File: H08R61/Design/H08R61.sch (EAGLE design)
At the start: 28 parts, among them P1 HEXABIT_17.32, U2 VL53L0X, X1 XTALL_CSTCE8M00G52

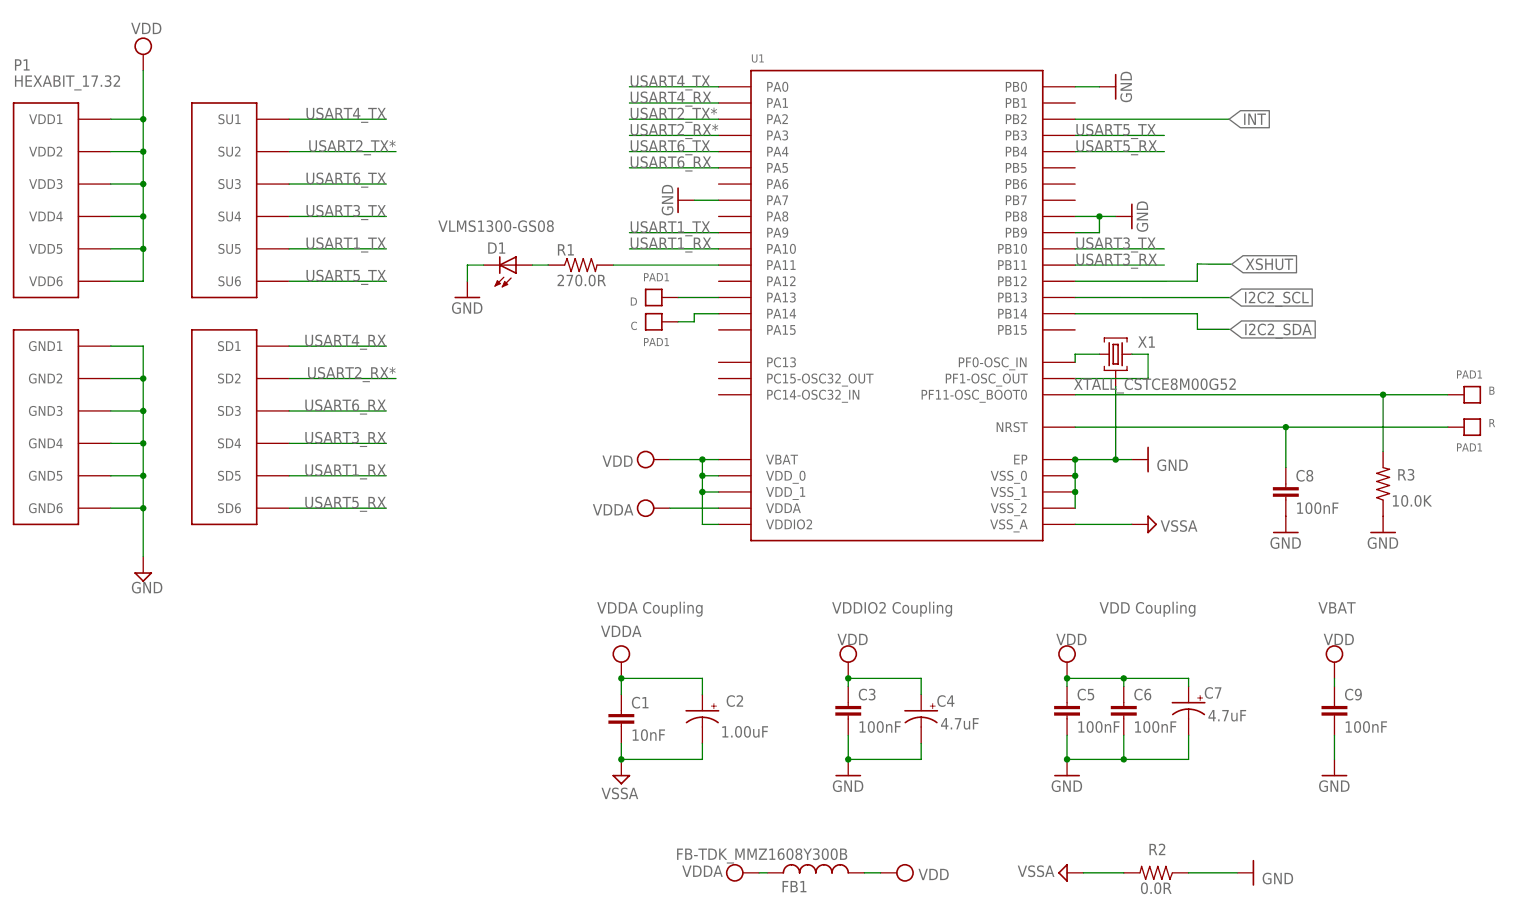
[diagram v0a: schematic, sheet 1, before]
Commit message: - Changing the MC to STM32G0 - Editing the electronic design to improve the performance
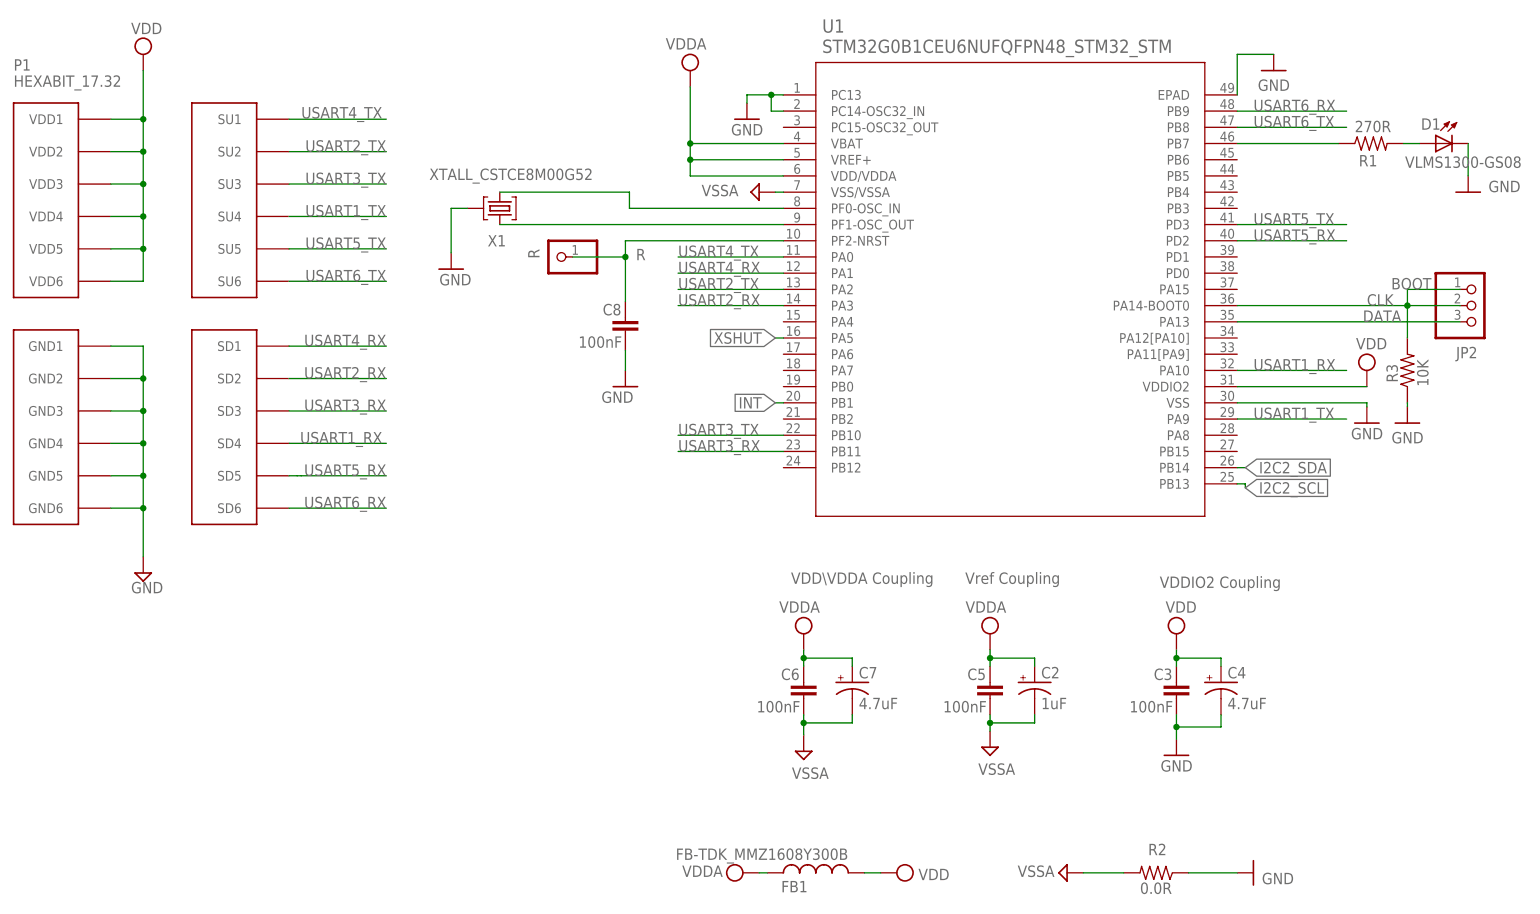
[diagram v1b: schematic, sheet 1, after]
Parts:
- removed B, C, D: PAD1, Hexabitz:PAD1
- removed C1: 10nF, Hexabitz:C-0603
- removed C9: 100nF, Hexabitz:C-0603
- removed R4: 2.2k, Hexabitz:R-0603
- added JP2: (no value), pinhead:PINHD-1X3
- added R8: 10k, HEXABITZ_RCLS:R-0603
- C10: device Hexabitz:C-0603 -> HEXABITZ_RCLS:C-0603; CAPACITANCE 100 nF -> (none); MFN KEMET -> (none); MPN C0603C104K8RACTU -> (none); OCTOPART_URL https://octopart.com/0603yc104k4t2a-avx+interconnect+%2F+el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 -> (none); TOLERANCE ±10% -> (none); VOLTAGE_RATING 16.0 V -> (none)
- C11: device Hexabitz:C-0805 -> HEXABITZ_RCLS:C-0805-POL; CAPACITANCE 4.7µF -> (none); MFN Murata -> (none); MPN GRM21BC81E475KA12L -> (none); OCTOPART_URL https://octopart.com/grm21bc81e475ka12l-murata-10331911?r=s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 -> (none); TOLERANCE 10% -> (none); VOLTAGE_RATING 25V -> (none)
- C2: value 1.00uF -> 1uF; device Hexabitz:C-0805 -> HEXABITZ_RCLS:C-0805-POL; CAPACITANCE 1.00uF -> (none); MFN Yageo -> (none); MPN CC0805KKX7R7BB105 -> (none); OCTOPART_URL https://octopart.com/cc0805kkx7r7bb105-yageo-8376555?r=sp&s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 -> (none); TOLERANCE 10% -> (none); VOLTAGE_RATING 16V -> (none)
- C3, C6, C8: device Hexabitz:C-0603 -> HEXABITZ_RCLS:C-0603; CAPACITANCE 100nF -> (none); MFN KEMET -> (none); MPN C0603C104K8RACTU -> (none); OCTOPART_URL https://octopart.com/c0603c104k8ractu-kemet-145075?r=sp&s=9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 -> (none); TOLERANCE 10% -> (none); VOLTAGE_RATING 10V -> (none)
- C4, C7: device Hexabitz:C-0805 -> HEXABITZ_RCLS:C-0805-POL; CAPACITANCE 4.7uF -> (none); MFN Murata -> (none); MPN GRM21BC81E475KA12L -> (none); OCTOPART_URL https://octopart.com/grm21bc81e475ka12l-murata-10331911?r=s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 -> (none); TOLERANCE 10% -> (none); VOLTAGE_RATING 25V -> (none)
- C5: device Hexabitz:C-0603 -> HEXABITZ_RCLS:C-0603; CAPACITANCE 100nF -> (none); MFN KEMET -> (none); MPN C0603C104K8RACTU -> (none); OCTOPART_URL https://octopart.com/c0603c104k8ractu-kemet-145075?r=sp&s=9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 -> (none); TOLERANCE 10% -> (none); VOLTAGE_RATING 10 -> (none)
- FB1: device Hexabitz:FB-TDK_MMZ1608Y300B -> HEXABITZ_RCLS:FB-TDK_MMZ1608Y300B
- R: value PAD1 -> R; device Hexabitz:PAD1 -> HEXABITZ_USER_INTERFACE_PARTS:PINHD-1X1
- R1: value 270.0R -> 270R; device Hexabitz:R-0603 -> HEXABITZ_RCLS:R-0603; MFN Yageo -> (none); MPN RC0603FR-07270RL -> (none); OCTOPART_URL https://octopart.com/erj-3geyj271v-panasonic-55560546 -> (none); RESISTANCE 270.0 Ohm -> (none); TOLERANCE 1% -> (none)
- R2: device Hexabitz:R-0603 -> HEXABITZ_RCLS:R-0603; OCTOPART_URL https://octopart.com/crcw06030000z0eahp-vishay-44320230 -> https://octopart.com/rc0603jr-070rl-yageo-1241539?r=sp&s=X2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
- R3: value 10.0K -> 10K; device Hexabitz:R-0603 -> HEXABITZ_RCLS:R-0603; MFN Yageo -> (none); MPN RC0603JR-0710KL -> (none); OCTOPART_URL https://octopart.com/crcw060310k0jneb-vishay+dale-46603268 -> (none); RESISTANCE 10.0K Ohm -> (none); TOLERANCE 5% -> (none)
- R5, R6: device Hexabitz:R-0603 -> HEXABITZ_RCLS:R-0603; MFN Yageo -> (none); MPN RC0603FR-07270RL -> (none); OCTOPART_URL https://octopart.com/crcw06032k20fkea-vishay-40018987 -> (none); RESISTANCE 2.2 kΩ -> (none); TOLERANCE ±1% -> (none)
- R7: value 2.2k -> 10k; device Hexabitz:R-0603 -> HEXABITZ_RCLS:R-0603; MFN Yageo -> (none); MPN RC0603FR-07270RL -> (none); OCTOPART_URL https://octopart.com/crcw06032k20fkea-vishay-40018987 -> (none); RESISTANCE 2.2 kΩ -> (none); TOLERANCE ±1% -> (none)
- U1: value (none) -> STM32G0B1CEU6NUFQFPN48_STM32_STM; device Hexabitz:STM32F091CBU6 -> HEXABITZ_ICs:STM32G0B1CEU6NUFQFPN48_STM32_STM
- U2: device Hexabitz:VL53L0X -> HEXABITZ_ICs:VL53L0X
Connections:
- net USART2_RX* renamed USART2_RX
- net USART2_TX* renamed USART2_TX
- removed net AGND: C10.2, C11.-, U2.AVSSVCSEL, U2.GND
- removed net B1: B.P$1, R3.2, U1.PF11-OSC_BOOT0
- removed net N$9: C.P$1, U1.PA14
- removed net R1: C8.1, R.P$1, U1.NRST
- new net CLK: JP2.1, JP2.2, R3.2, U1.PA14-BOOT0
- new net DATA: JP2.3, U1.PA13
- net GND: now also C10.2, C11.-, U1.EPAD, U1.PC13, U1.PC14-OSC32_IN, U1.VSS, U2.AVSSVCSEL, U2.GND; no longer C5.2, C6.2, C7.-, C9.2, U1.EP, U1.PA7, U1.PB0, U1.PB8, U1.PB9, U1.VSS_0, U1.VSS_1, U1.VSS_2
- net I2C2_SCL: now also R6.1; no longer R5.1
- net I2C2_SDA: now also R5.1; no longer R6.1
- net INT: now also R8.1, U1.PB1; no longer R7.1, U1.PB2
- net N$3: now also D1.A; no longer U1.PA11
- net N$4: now also C8.1, R.1, U1.PF2-NRST; no longer D1.A, R1.1
- net N$5: now also U1.PF1-OSC_OUT; no longer U1.PF0-OSC_IN
- net N$6: now also U1.PF0-OSC_IN; no longer U1.PF1-OSC_OUT
- net N$7: now also R1.1, U1.PB7; no longer D.P$1, U1.PA13
- net USART1_RX: now also P1.SD4; no longer P1.SD5
- net USART1_TX: now also P1.SU4; no longer P1.SU5
- net USART3_RX: now also P1.SD3; no longer P1.SD4
- net USART3_TX: now also P1.SU3; no longer P1.SU4
- net USART5_RX: now also P1.SD5, U1.PD2; no longer P1.SD6, U1.PB4
- net USART5_TX: now also P1.SU5, U1.PD3; no longer P1.SU6, U1.PB3
- net USART6_RX: now also P1.SD6, U1.PB9; no longer P1.SD3, U1.PA5
- net USART6_TX: now also P1.SU6, U1.PB8; no longer P1.SU3, U1.PA4
- net VDD: now also R8.2; no longer C10.1, C11.+, C5.1, C6.1, C7.+, C9.1, R4.2, U1.VBAT, U1.VDD_0, U1.VDD_1, U2.AVDD, U2.AVDDVCSEL
- net VDDA: now also C10.1, C11.+, C5.1, C6.1, C7.+, U1.VBAT, U1.VDD/VDDA, U1.VREF+, U2.AVDD, U2.AVDDVCSEL; no longer C1.1, U1.VDDA
- net VSSA: now also C5.2, C6.2, C7.-, U1.VSS/VSSA; no longer C1.2, U1.VSS_A
- net XSHUT: now also R7.1, U1.PA5; no longer R4.1, U1.PB12
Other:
- note added: "BOOT"
- note added: "H08R61"
- note added: "H08R61_Backend"
- note added: "H08R61_Frontend"
- note added: "IR ToF LiDar Sensor"
- note added: "Subhi Kalzie"
- note added: "VDD=3.3 Volts"
- note added: "VDD\VDDA Coupling"
- note added: "Vref Coupling"
- note removed: "0"
- note removed: "Anas Kaadan"
- note removed: "H08R6"
- note removed: "H08R6_Backend"
- note removed: "H08R6_Frontend"
- note removed: "Time-of-Flight IR Sensor"
- note removed: "VBAT"
- note removed: "VDD Coupling"
- note removed: "VDDA Coupling"
- moved on the sheet: C10, C11, C2, C3, C4, C5, C6, C7, C8, D1, R1, R3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
